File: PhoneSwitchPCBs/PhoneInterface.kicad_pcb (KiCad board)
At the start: 2 copper layers, 99.2 x 36.1 mm, 52 parts, among them J1 Interface, J2 6P2C, K1 EC2-5NU, K2 EC2-5NU, K3 EC2-5NU, K4 EC2-5NU, K5 EC2-5NU, Q1 PHPT61003PYX, Q2 PHPT61003NYX, Q3 XP231N02013R-G, Q4 XP231N02013R-G, Q5 XP231N02013R-G, Q6 XP231N02013R-G, U1 TCMD1000, U2 NL17SZ14DBVT1G

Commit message: More progress to PCB Layout
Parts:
- R6, R7: moved to B.Cu
- moved R6 143.7 mm to (157.7, 100.5), turned to 90 degrees
- moved R7 137.9 mm to (147.6, 100.5), turned to 90 degrees
- moved K1 66.0 mm to (111.5, 104.0), turned to 270 degrees
- moved K5 38.6 mm to (111.5, 94.1), turned to 270 degrees
- moved K2 35.0 mm to (137.4, 94.4)
- moved K3 34.6 mm to (150.0, 94.4)
- moved C5 34.4 mm to (123.7, 137.4)
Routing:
- net Net-(K1-Pad9): track 0.00 -> 46.2 mm
- net Net-(K2-Pad10): track 0.00 -> 40.7 mm
- net Net-(K2-Pad3): track 0.00 -> 39.6 mm
- net Net-(K1-Pad4): track 0.00 -> 36.2 mm
- net Net-(J1-Pad1): track 0.00 -> 29.8 mm
- net Net-(J1-Pad3): track 0.00 -> 29.7 mm
- net Net-(J1-Pad2): track 0.00 -> 27.3 mm
- net /AUDR: track 0.00 -> 20.7 mm
- net Net-(J1-Pad6): track 0.00 -> 19.5 mm
- net Net-(J1-Pad4): track 0.00 -> 18.4 mm
- net Net-(J1-Pad7): track 0.00 -> 16.6 mm
- net Net-(K2-Pad9): track 0.00 -> 13.6 mm
- net Net-(K2-Pad4): track 0.00 -> 13.6 mm
- net Net-(J1-Pad5): track 0.00 -> 12.9 mm
- net /AUDT: track 0.00 -> 11.7 mm
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
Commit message: Mostly finish trace routing.
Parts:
- Q5, Q6, R11, R13, R15, R16, R17, R18: moved to B.Cu
- moved R11 140.4 mm to (156.8, 88.8)
- moved R13 126.5 mm to (158.8, 91.7), turned to 180 degrees
- moved R18 124.2 mm to (133.0, 96.7)
- moved R16 104.9 mm to (133.0, 98.8)
- moved R17 101.2 mm to (115.4, 114.0)
- moved Q3 99.8 mm to (158.5, 92.7), turned to 90 degrees
- moved R15 90.1 mm to (115.4, 111.7)
- moved R19 82.2 mm to (96.1, 99.2), turned to 270 degrees
- moved Q6 57.7 mm to (133.4, 92.8), turned to 90 degrees
- moved Q5 49.5 mm to (111.5, 113.0), turned to 90 degrees
- moved D5 47.0 mm to (147.1, 91.4)
- moved D4 46.8 mm to (144.8, 91.4), turned to 180 degrees
- moved D9 44.6 mm to (116.0, 97.3), turned to 270 degrees
- moved C5 30.4 mm to (121.8, 107.1)
- moved J1 0.53 mm to (90.9, 112.3)
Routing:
- net /RTRIP: track 0.00 -> 61.4 mm, vias 0 -> 1
- net /RINGE: track 0.00 -> 40.3 mm, vias 0 -> 1
- net /CINST: track 0.00 -> 14.8 mm
- net Net-(D4-Pad2): track 0.00 -> 10.4 mm
- net Net-(Q3-Pad1): track 0.00 -> 9.17 mm, vias 0 -> 1
- net +5V: track 11.3 -> 19.3 mm
- net Net-(D5-Pad2): track 0.00 -> 6.89 mm
- net +3V3: track 2.20 -> 8.91 mm
- net GND: track 27.4 -> 33.4 mm, vias 2 -> 3
- net /LTSW: track 11.3 -> 17.3 mm
- net Net-(Q6-Pad1): track 0.00 -> 4.73 mm
- net Net-(Q5-Pad1): track 0.00 -> 4.71 mm
- net Net-(J1-Pad6): track 19.5 -> 20.2 mm
- net Net-(J1-Pad1): track 29.8 -> 29.2 mm

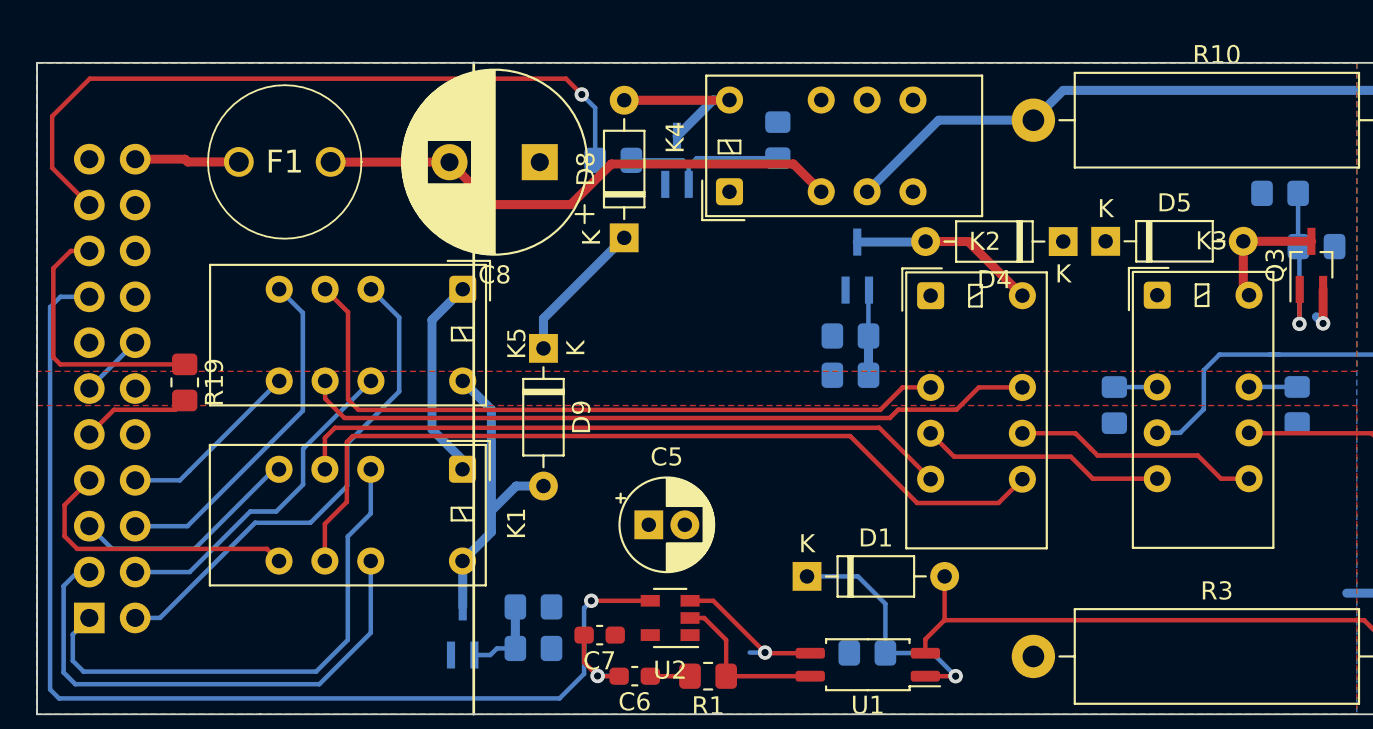
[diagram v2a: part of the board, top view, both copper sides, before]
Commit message: tweaked detect resistor to pulldown, finished routing all tracks!
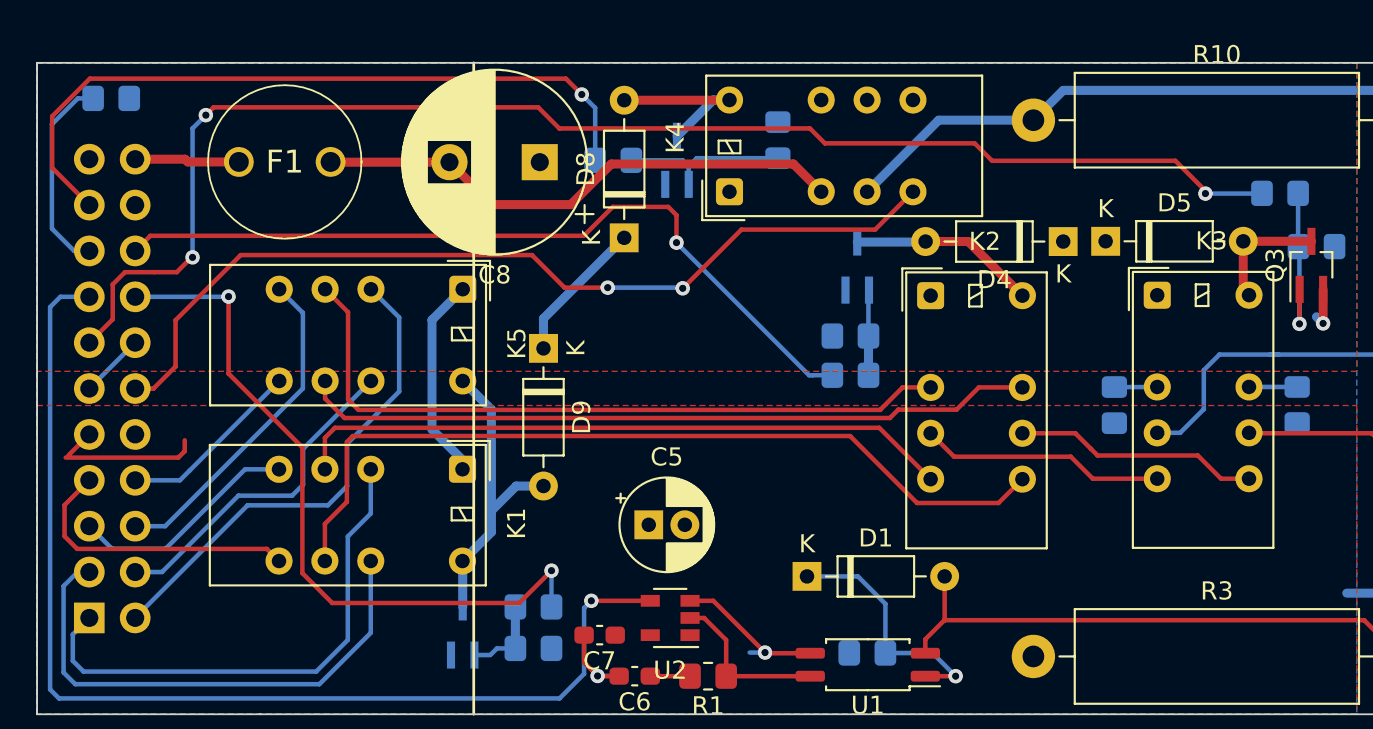
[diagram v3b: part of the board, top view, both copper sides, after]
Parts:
- R19: value 1k -> 4.7k; moved to B.Cu
- moved R19 16.2 mm to (92.1, 83.5), turned to 0 degrees
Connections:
- R19 pad 2: +3V3 -> GND
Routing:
- net /AUDE: track 0.00 -> 77.7 mm, vias 0 -> 3
- net /VRING: track 0.00 -> 50.6 mm, vias 0 -> 2
- net /LINE: track 0.00 -> 44.8 mm, vias 0 -> 1
- net /LTSEL: track 0.00 -> 39.4 mm, vias 0 -> 2
- net /CINST: track 14.8 -> 11.2 mm
- net +3V3: track 8.91 -> 11.2 mm
- net Net-(J1-Pad6): track 20.2 -> 19.4 mm

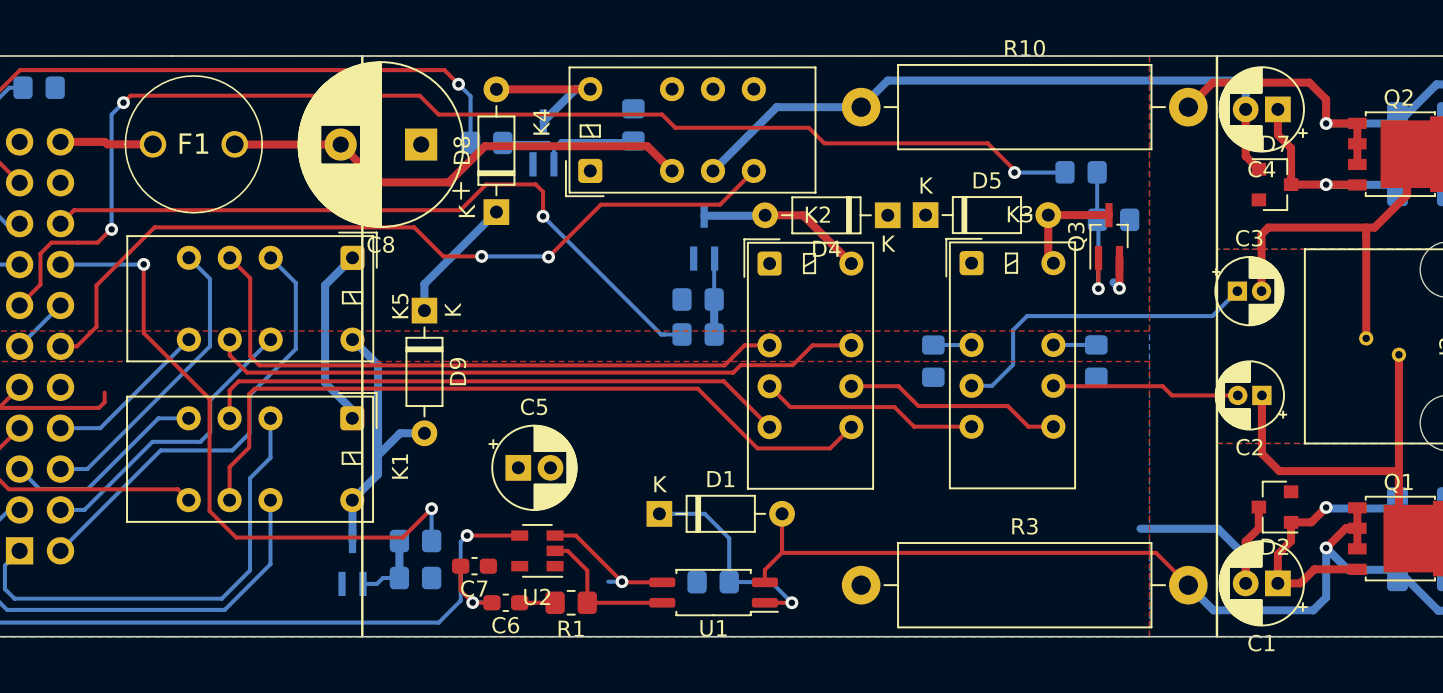
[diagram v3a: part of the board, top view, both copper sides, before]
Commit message: Remove extra cap from schematic, finish up PCB design
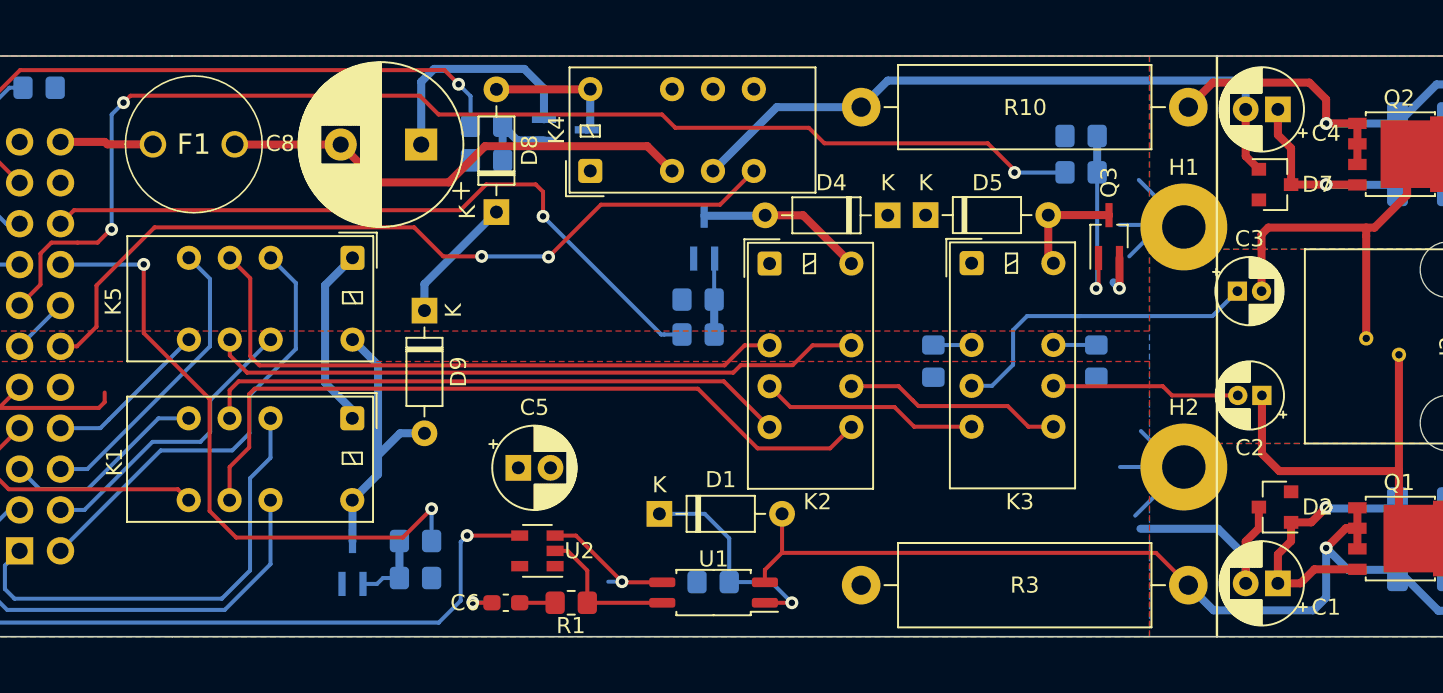
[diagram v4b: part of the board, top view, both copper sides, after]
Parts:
- removed C7: .1u, Capacitor_SMD:C_0603_1608Metric_Pad1.08x0.95mm_HandSolder
- added H1: MNT1, MountingHole:MountingHole_2.7mm_M2.5_Pad, F.Cu at (163.2, 92.2)
- added H2: MNT2, MountingHole:MountingHole_2.7mm_M2.5_Pad, F.Cu at (163.2, 107.1)
- F1: value 100mA Slow Blow -> 100mA
- moved R14 9.38 mm to (119.9, 88.0), turned to 0 degrees
- moved R13 5.58 mm to (156.8, 86.5), turned to 0 degrees
- moved Q4 1.59 mm to (124.8, 86.1), turned to 0 degrees
- moved R12 1.07 mm to (119.9, 85.9)
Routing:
- net GND: track 33.4 -> 69.5 mm
- net Net-(Q4-Pad1): track 9.44 -> 5.09 mm
- net Net-(Q3-Pad1): track 9.17 -> 11.5 mm
- net Net-(D8-Pad2): track 9.58 -> 8.45 mm
- net /RINGE: track 40.3 -> 39.2 mm
